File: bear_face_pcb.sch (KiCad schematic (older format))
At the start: 201 parts, among them J1 TYPE-C-31-M-12, J2 Conn_02x03_Odd_Even, SW1 RESET, U1 ATmega32U4-AU, U2 SRV05-4, Y1 16MHz

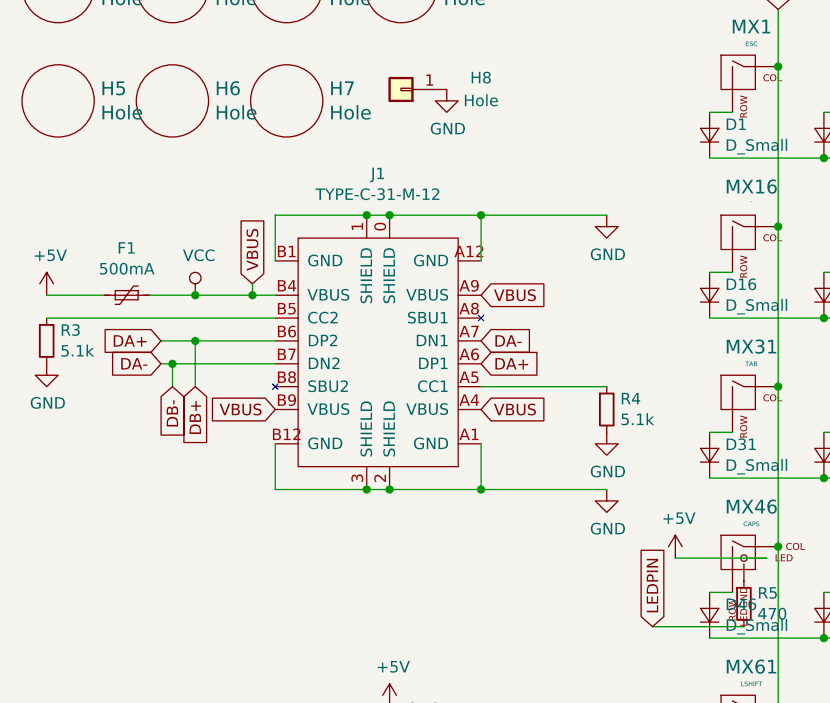
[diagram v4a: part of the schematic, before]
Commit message: replaced usb micro
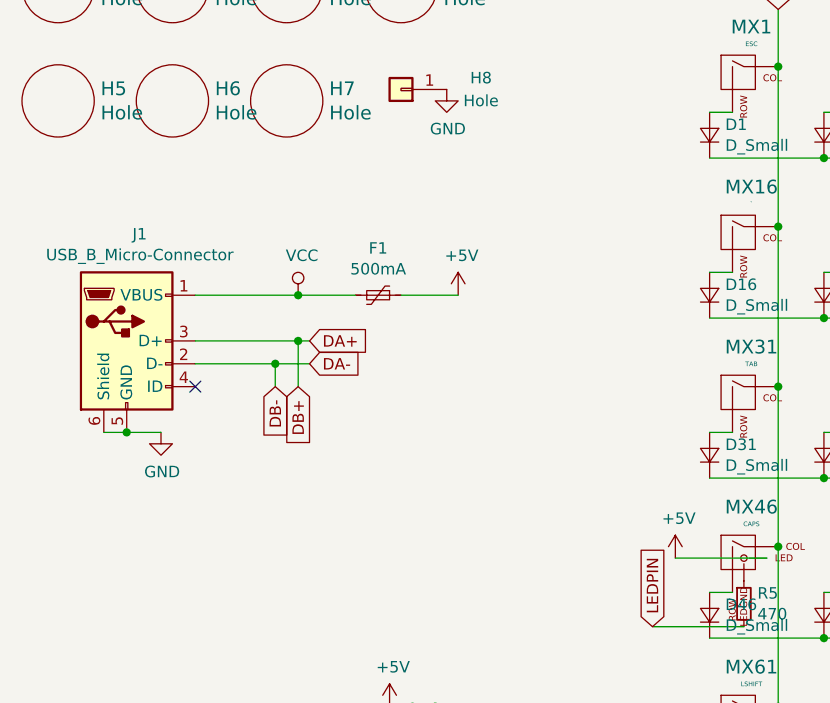
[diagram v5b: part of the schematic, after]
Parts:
- removed J1: TYPE-C-31-M-12, bear_face_parts:USB-C_SMD-TYPE-C-31-M-12, symbol bear_face_pcb:TYPE-C-31-M-12
- removed R3, R4: 5.1k, Resistor_SMD:R_0805_2012Metric, symbol Device:R_Small
- added J1: USB_B_Micro-Connector, Connector_USB:USB_Micro-B_Wuerth_629105150521, symbol bear_face_pcb:USB_B_Micro-Connector
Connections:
- net +5V: now also F1.1; no longer F1.2
- net DA+: now also J1.3 (D+)
- net DA-: now also J1.2 (D-)
- net GND: now also J1.5 (GND), J1.6 (Shield)
- net VCC: now also F1.2, J1.1 (VBUS); no longer F1.1
- no-connect marks 3 -> 4
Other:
- moved on the sheet: F1
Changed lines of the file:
@@
-	1    0    0    -1
-$EndComp
-$Comp
-L Device:R_Small R3
-U 1 1 65B37F14
-P 650 2250
-F 0 "R3" H 709 2296 50  0000 L CNN
-F 1 "5.1k" H 709 2205 50  0000 L CNN
-F 2 "Resistor_SMD:R_0805_2012Metric" H 650 2250 50  0001 C CNN
-F 3 "~" H 650 2250 50  0001 C CNN
-F 4 "C2907269" H 650 2250 50  0001 C CNN "LCSC"
-	1    650  2250
-	1    0    0    -1
-$EndComp
-$Comp
-L Device:R_Small R4
-U 1 1 65B89020
-P 3100 2550
-F 0 "R4" H 3159 2596 50  0000 L CNN
-F 1 "5.1k" H 3159 2505 50  0000 L CNN
-F 2 "Resistor_SMD:R_0805_2012Metric" H 3100 2550 50  0001 C CNN
-F 3 "~" H 3100 2550 50  0001 C CNN
-F 4 "C2907269" H 3100 2550 50  0001 C CNN "LCSC"
-	1    3100 2550
-	1    0    0    -1
-$EndComp
-$Comp
-L power:GND #PWR0110
-U 1 1 65BFFB57
-P 650 2350
-F 0 "#PWR0110" H 650 2100 50  0001 C CNN
-F 1 "GND" H 655 2177 50  0000 C CNN
-F 2 "" H 650 2350 50  0001 C CNN
-F 3 "" H 650 2350 50  0001 C CNN
-	1    650  2350
 	1    0    0    -1
 $EndComp
@@
 	2250 3850 2150 3850
 Connection ~ 2250 3850
-Wire Wire Line
-	650  2050 900  2050
 $Comp
 L power:+5V #PWR03
 U 1 1 5E226273
-P 650 2050
-F 0 "#PWR03" H 650 1900 50  0001 C CNN
-F 1 "+5V" H 665 2223 50  0000 C CNN
-F 2 "" H 650 2050 50  0001 C CNN
-F 3 "" H 650 2050 50  0001 C CNN
-	1    650  2050
+P 2450 2050
+F 0 "#PWR03" H 2450 1900 50  0001 C CNN
+F 1 "+5V" H 2465 2223 50  0000 C CNN
+F 2 "" H 2450 2050 50  0001 C CNN
+F 3 "" H 2450 2050 50  0001 C CNN
+	1    2450 2050
 	1    0    0    -1
 $EndComp
@@
 L Device:Polyfuse_Small F1
 U 1 1 5E21E2B0
-P 1000 2050
-F 0 "F1" V 795 2050 50  0000 C CNN
-F 1 "500mA" V 886 2050 50  0000 C CNN
-F 2 "Fuse:Fuse_1206_3216Metric" H 1050 1850 50  0001 L CNN
-F 3 "~" H 1000 2050 50  0001 C CNN
-F 4 "C70076" V 1000 2050 50  0001 C CNN "LCSC"
-	1    1000 2050
+P 2100 2050
+F 0 "F1" V 1895 2050 50  0000 C CNN
+F 1 "500mA" V 1986 2050 50  0000 C CNN
+F 2 "Fuse:Fuse_1206_3216Metric" H 2150 1850 50  0001 L CNN
+F 3 "~" H 2100 2050 50  0001 C CNN
+F 4 "C70076" V 2100 2050 50  0001 C CNN "LCSC"
+	1    2100 2050
 	0    1    1    0
 $EndComp
@@
 	1    0    0    -1
 $EndComp
-Wire Wire Line
-	1300 2050 1100 2050
-Connection ~ 1300 2050
 $Comp
 L power:VCC #PWR02
 U 1 1 5E224EBD
-P 1300 2050
-F 0 "#PWR02" H 1300 1900 50  0001 C CNN
-F 1 "VCC" H 1317 2223 50  0000 C CNN
-F 2 "" H 1300 2050 50  0001 C CNN
-F 3 "" H 1300 2050 50  0001 C CNN
-	1    1300 2050
-	1    0    0    -1
-$EndComp
-$Comp
-L bear_face_pcb:TYPE-C-31-M-12 J1
-U 1 1 65565029
-P 2100 2300
-F 0 "J1" H 2100 3081 50  0000 C CNN
-F 1 "TYPE-C-31-M-12" H 2100 2990 50  0000 C CNN
-F 2 "bear_face_parts:USB-C_SMD-TYPE-C-31-M-12" H 2100 3350 50  0001 C CNN
-F 3 "" H 2100 3350 50  0001 C CNN
-F 4 "C165948" H 2100 2300 50  0001 C CNN "LCSC"
-	1    2100 2300
-	1    0    0    -1
-$EndComp
-Wire Wire Line
-	1650 1900 1650 1700
-Wire Wire Line
-	1650 1700 2050 1700
-Wire Wire Line
-	2550 1700 2550 1900
-Connection ~ 2050 1700
-Wire Wire Line
-	2050 1700 2150 1700
-Connection ~ 2150 1700
-Wire Wire Line
-	2150 1700 2550 1700
-Wire Wire Line
-	1650 2700 1650 2900
-Wire Wire Line
-	1650 2900 2050 2900
-Wire Wire Line
-	2550 2900 2550 2700
-Connection ~ 2050 2900
-Wire Wire Line
-	2050 2900 2150 2900
-Connection ~ 2150 2900
-Wire Wire Line
-	2150 2900 2550 2900
-Wire Wire Line
-	2550 1700 3100 1700
-Connection ~ 2550 1700
-Wire Wire Line
-	2550 2900 3100 2900
-Connection ~ 2550 2900
+P 1750 2050
+F 0 "#PWR02" H 1750 1900 50  0001 C CNN
+F 1 "VCC" H 1767 2223 50  0000 C CNN
+F 2 "" H 1750 2050 50  0001 C CNN
+F 3 "" H 1750 2050 50  0001 C CNN
+	1    1750 2050
+	1    0    0    -1
+$EndComp
+Text GLabel 1800 2350 2    50   Input ~ 0
+DA-
+Text GLabel 1800 2250 2    50   Input ~ 0
+DA+
+Text GLabel 1650 2450 3    50   Input ~ 0
+DB-
+Text GLabel 1750 2450 3    50   Input ~ 0
+DB+
+Wire Wire Line
+	1800 2350 1650 2350
+Wire Wire Line
+	1800 2250 1750 2250
+Wire Wire Line
+	1650 2450 1650 2350
+Connection ~ 1750 2250
+Wire Wire Line
+	1750 2250 1300 2250
+Wire Wire Line
+	1750 2450 1750 2250
+Connection ~ 1650 2350
+Wire Wire Line
+	1650 2350 1300 2350
+Wire Wire Line
+	1350 5150 1750 5150
+Wire Wire Line
+	1350 5250 1750 5250
+$Comp
+L bear_face_pcb:USB_B_Micro-Connector J1
+U 1 1 6554DB7C
+P 1000 2250
+F 0 "J1" H 1057 2717 50  0000 C CNN
+F 1 "USB_B_Micro-Connector" H 1057 2626 50  0000 C CNN
+F 2 "Connector_USB:USB_Micro-B_Wuerth_629105150521" H 1150 2200 50  0001 C CNN
+F 3 "" H 1150 2200 50  0001 C CNN
+	1    1000 2250
+	1    0    0    -1
+$EndComp
+Wire Wire Line
+	1300 2050 1750 2050
+Wire Wire Line
+	2200 2050 2450 2050
+Connection ~ 1750 2050
+Wire Wire Line
+	1750 2050 2000 2050
+NoConn ~ 1300 2450
+Wire Wire Line
+	900  2650 1000 2650
+Connection ~ 1000 2650
+Wire Wire Line
+	1000 2650 1150 2650
 $Comp
 L power:GND #PWR0101
-U 1 1 656E6904
-P 3100 1700
-F 0 "#PWR0101" H 3100 1450 50  0001 C CNN
-F 1 "GND" H 3105 1527 50  0000 C CNN
-F 2 "" H 3100 1700 50  0001 C CNN
-F 3 "" H 3100 1700 50  0001 C CNN
-	1    3100 1700
-	1    0    0    -1
-$EndComp
-$Comp
-L power:GND #PWR0102
-U 1 1 656E8BE8
-P 3100 2900
-F 0 "#PWR0102" H 3100 2650 50  0001 C CNN
-F 1 "GND" H 3105 2727 50  0000 C CNN
-F 2 "" H 3100 2900 50  0001 C CNN
-F 3 "" H 3100 2900 50  0001 C CNN
-	1    3100 2900
-	1    0    0    -1
-$EndComp
-Wire Wire Line
-	2550 2450 3100 2450
-$Comp
-L power:GND #PWR0108
-U 1 1 65757791
-P 3100 2650
-F 0 "#PWR0108" H 3100 2400 50  0001 C CNN
-F 1 "GND" H 3105 2477 50  0000 C CNN
-F 2 "" H 3100 2650 50  0001 C CNN
-F 3 "" H 3100 2650 50  0001 C CNN
-	1    3100 2650
-	1    0    0    -1
-$EndComp
-Text GLabel 1150 2250 0    50   Input ~ 0
-DA+
-Text GLabel 2550 2350 2    50   Input ~ 0
-DA+
-Text GLabel 1150 2350 0    50   Input ~ 0
-DA-
-Text GLabel 2550 2250 2    50   Input ~ 0
-DA-
-Text GLabel 1550 2000 1    50   Input ~ 0
-VBUS
-Text GLabel 2550 2050 2    50   Input ~ 0
-VBUS
-Text GLabel 2550 2550 2    50   Input ~ 0
-VBUS
-Text GLabel 1650 2550 0    50   Input ~ 0
-VBUS
-Wire Wire Line
-	1550 2000 1550 2050
-Wire Wire Line
-	1550 2050 1650 2050
-Wire Wire Line
-	1300 2050 1550 2050
-Connection ~ 1550 2050
-Text GLabel 1200 2450 3    50   Input ~ 0
-DB-
-Text GLabel 1300 2450 3    50   Input ~ 0
-DB+
-Wire Wire Line
-	1150 2250 1300 2250
-Wire Wire Line
-	1150 2350 1200 2350
-Wire Wire Line
-	1200 2450 1200 2350
-Connection ~ 1200 2350
-Wire Wire Line
-	1200 2350 1650 2350
-Wire Wire Line
-	1300 2450 1300 2250
-Connection ~ 1300 2250
-Wire Wire Line
-	1300 2250 1650 2250
-Wire Wire Line
-	1350 5150 1750 5150
-Wire Wire Line
-	1350 5250 1750 5250
-Wire Wire Line
-	650  2150 1650 2150
+U 1 1 6578DF34
+P 1150 2650
+F 0 "#PWR0101" H 1150 2400 50  0001 C CNN
+F 1 "GND" H 1155 2477 50  0000 C CNN
+F 2 "" H 1150 2650 50  0001 C CNN
+F 3 "" H 1150 2650 50  0001 C CNN
+	1    1150 2650
+	1    0    0    -1
+$EndComp
 $EndSCHEMATC

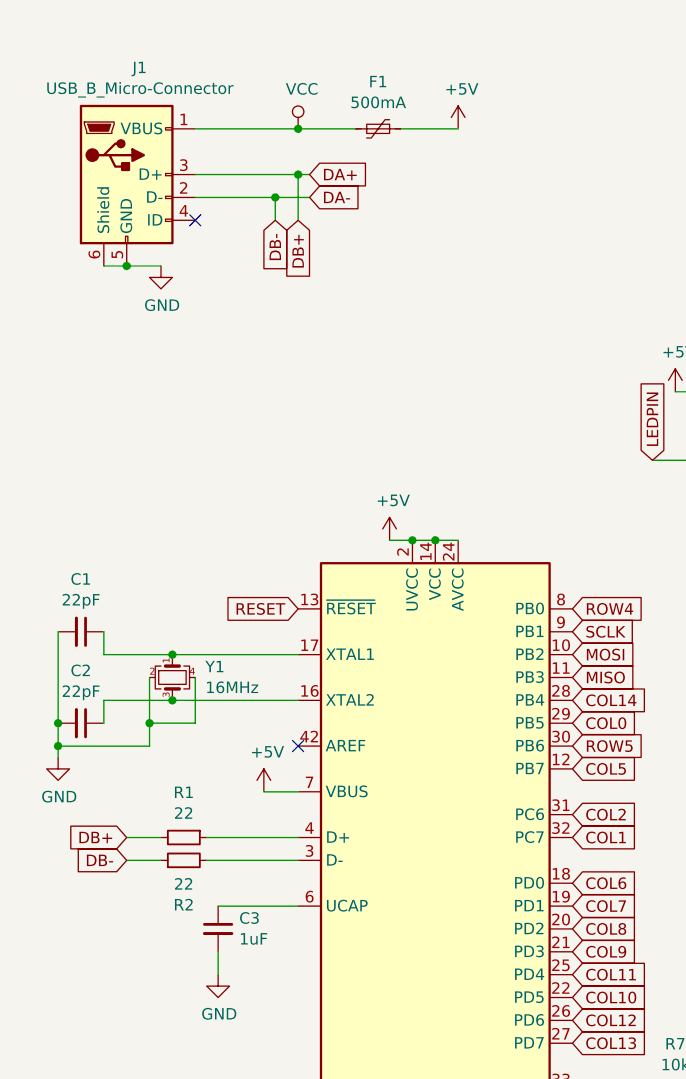
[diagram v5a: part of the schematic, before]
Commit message: pulled up to v3c route/via changes + * replaced micro usb * placed components for diff pairs
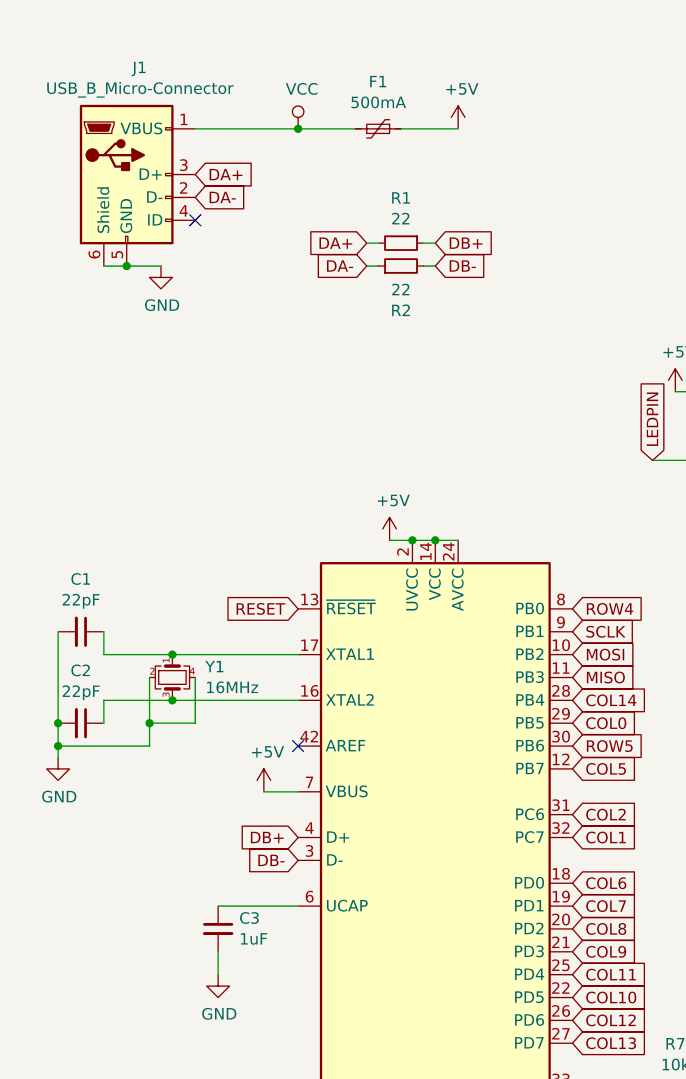
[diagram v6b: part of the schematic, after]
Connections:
- net DB-: now reaches R2.2, U1.3 (D-)
- net DB+: now reaches R1.1, U1.4 (D+)
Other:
- moved on the sheet: R1, R2
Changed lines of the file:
@@
 L Device:R_Small R1
 U 1 1 66036275
-P 1250 5150
-F 0 "R1" V 1054 5150 50  0000 C CNN
-F 1 "22" V 1145 5150 50  0000 C CNN
-F 2 "Resistor_SMD:R_0805_2012Metric" H 1250 5150 50  0001 C CNN
-F 3 "~" H 1250 5150 50  0001 C CNN
-F 4 "C17561" V 1250 5150 50  0001 C CNN "LCSC"
-	1    1250 5150
+P 2200 2550
+F 0 "R1" V 2004 2550 50  0000 C CNN
+F 1 "22" V 2095 2550 50  0000 C CNN
+F 2 "Resistor_SMD:R_0805_2012Metric" H 2200 2550 50  0001 C CNN
+F 3 "~" H 2200 2550 50  0001 C CNN
+F 4 "C17561" V 2200 2550 50  0001 C CNN "LCSC"
+	1    2200 2550
 	0    1    1    0
 $EndComp
@@
 L Device:R_Small R2
 U 1 1 66037A5E
-P 1250 5250
-F 0 "R2" V 1054 5250 50  0000 C CNN
-F 1 "22" V 1145 5250 50  0000 C CNN
-F 2 "Resistor_SMD:R_0805_2012Metric" H 1250 5250 50  0001 C CNN
-F 3 "~" H 1250 5250 50  0001 C CNN
-F 4 "C17561" V 1250 5250 50  0001 C CNN "LCSC"
-	1    1250 5250
+P 2200 2650
+F 0 "R2" V 2004 2650 50  0000 C CNN
+F 1 "22" V 2095 2650 50  0000 C CNN
+F 2 "Resistor_SMD:R_0805_2012Metric" H 2200 2650 50  0001 C CNN
+F 3 "~" H 2200 2650 50  0001 C CNN
+F 4 "C17561" V 2200 2650 50  0001 C CNN "LCSC"
+	1    2200 2650
 	0    -1   -1   0
 $EndComp
-Text GLabel 1000 5250 0    50   Input ~ 0
+Text GLabel 1750 5250 0    50   Input ~ 0
 DB-
-Text GLabel 1000 5150 0    50   Input ~ 0
+Text GLabel 1750 5150 0    50   Input ~ 0
 DB+
-Wire Wire Line
-	1000 5150 1150 5150
-Wire Wire Line
-	1000 5250 1150 5250
 $Comp
 L Connector_Generic:Conn_01x01 H8
@@
 	1    0    0    -1
 $EndComp
-Text GLabel 1800 2350 2    50   Input ~ 0
+Text GLabel 1300 2350 2    50   Input ~ 0
 DA-
-Text GLabel 1800 2250 2    50   Input ~ 0
+Text GLabel 1300 2250 2    50   Input ~ 0
 DA+
-Text GLabel 1650 2450 3    50   Input ~ 0
+Text GLabel 2350 2650 2    50   Input ~ 0
 DB-
-Text GLabel 1750 2450 3    50   Input ~ 0
+Text GLabel 2350 2550 2    50   Input ~ 0
 DB+
-Wire Wire Line
-	1800 2350 1650 2350
-Wire Wire Line
-	1800 2250 1750 2250
-Wire Wire Line
-	1650 2450 1650 2350
-Connection ~ 1750 2250
-Wire Wire Line
-	1750 2250 1300 2250
-Wire Wire Line
-	1750 2450 1750 2250
-Connection ~ 1650 2350
-Wire Wire Line
-	1650 2350 1300 2350
-Wire Wire Line
-	1350 5150 1750 5150
-Wire Wire Line
-	1350 5250 1750 5250
 $Comp
 L bear_face_pcb:USB_B_Micro-Connector J1
@@
 	1    0    0    -1
 $EndComp
+Wire Wire Line
+	2300 2550 2350 2550
+Wire Wire Line
+	2300 2650 2350 2650
+Text GLabel 2050 2550 0    50   Input ~ 0
+DA+
+Text GLabel 2050 2650 0    50   Input ~ 0
+DA-
+Wire Wire Line
+	2050 2550 2100 2550
+Wire Wire Line
+	2050 2650 2100 2650
 $EndSCHEMATC

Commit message: silks tweaks
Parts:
- D1, D10, D11, D12, D13, D14, D15, D16, D17, D18, D19, D2, D20, D21, D22, D23, D24, D25, D26, D27, D28, D29, D3, D30, D31, D32, D33, D34, D35, D36, D37, D38, D39, D4, D40, D41, D42, D43, D44, D45, D46, D47, D48, D49, D5, D50, D51, D52, D53, D54, D55, D56, D57, D58, D59, D6, D60, D61, D62, D63, D64, D65, D66, D67, D68, D69, D7, D70, D71, D72, D73, D74, D75, D76, D77, D78, D79, D8, D80, D81, D82, D83, D84, D85, D9: footprint Diode_SMD:D_0805_2012Metric_Pad1.15x1.40mm_HandSolder -> bear_face_parts:D_0805_2012Metric_Pad1.15x1.40mm_HandSolder
